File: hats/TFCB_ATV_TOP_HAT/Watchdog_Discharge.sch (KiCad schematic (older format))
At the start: 24 parts

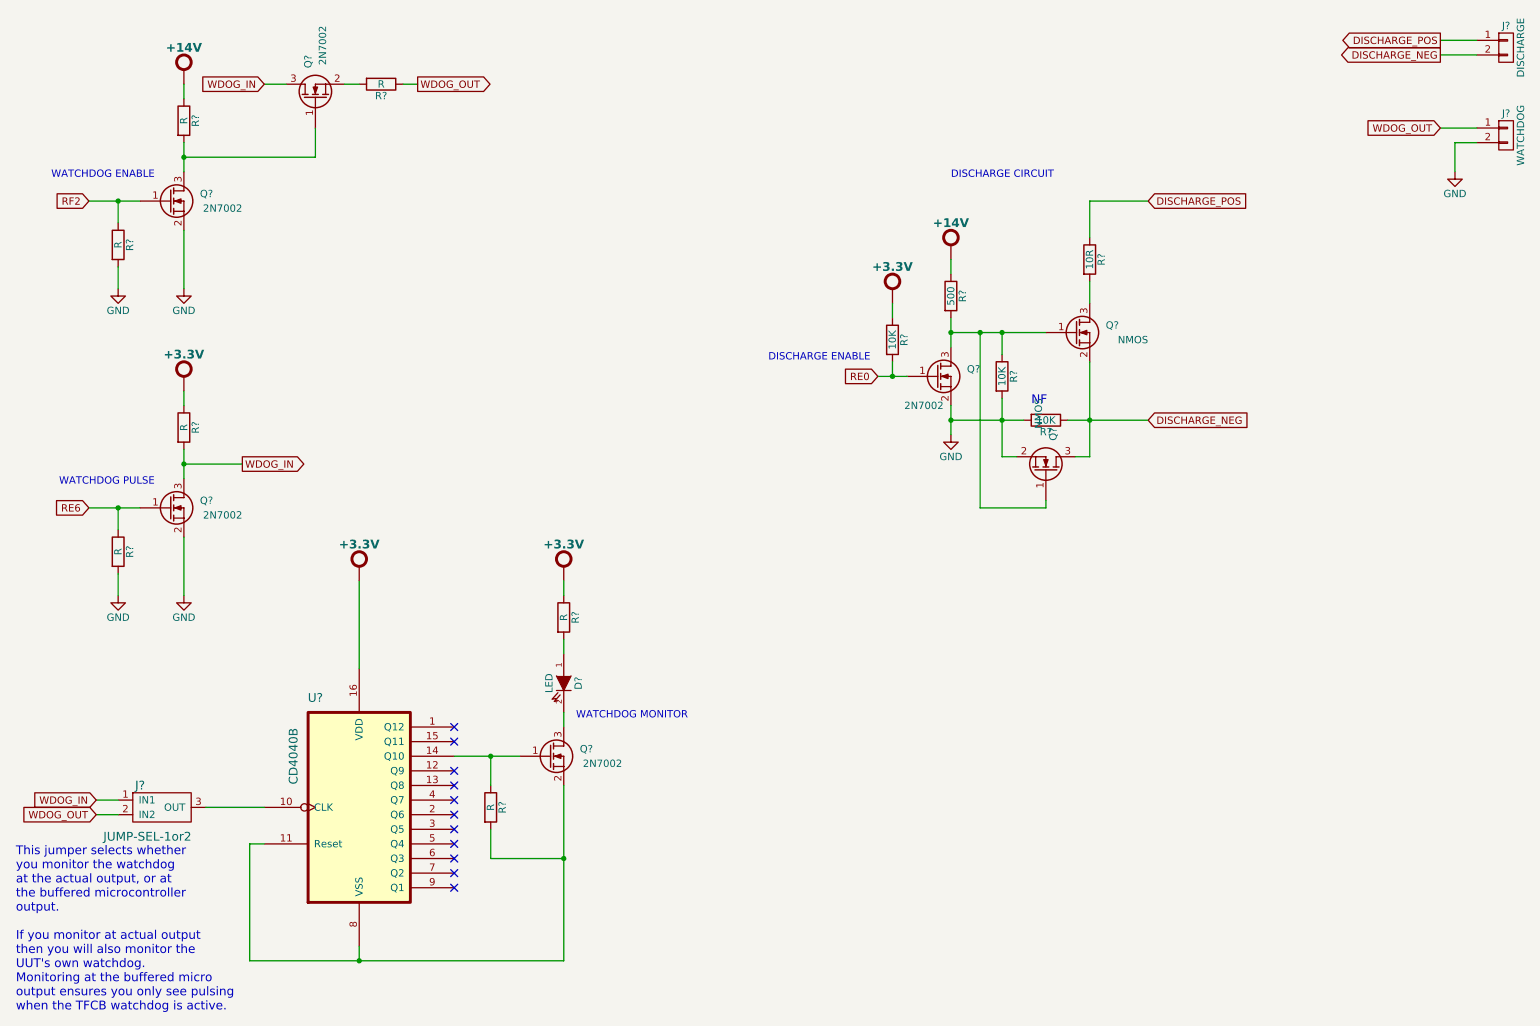
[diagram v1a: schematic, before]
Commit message: Added scanner trigger and current sense cct
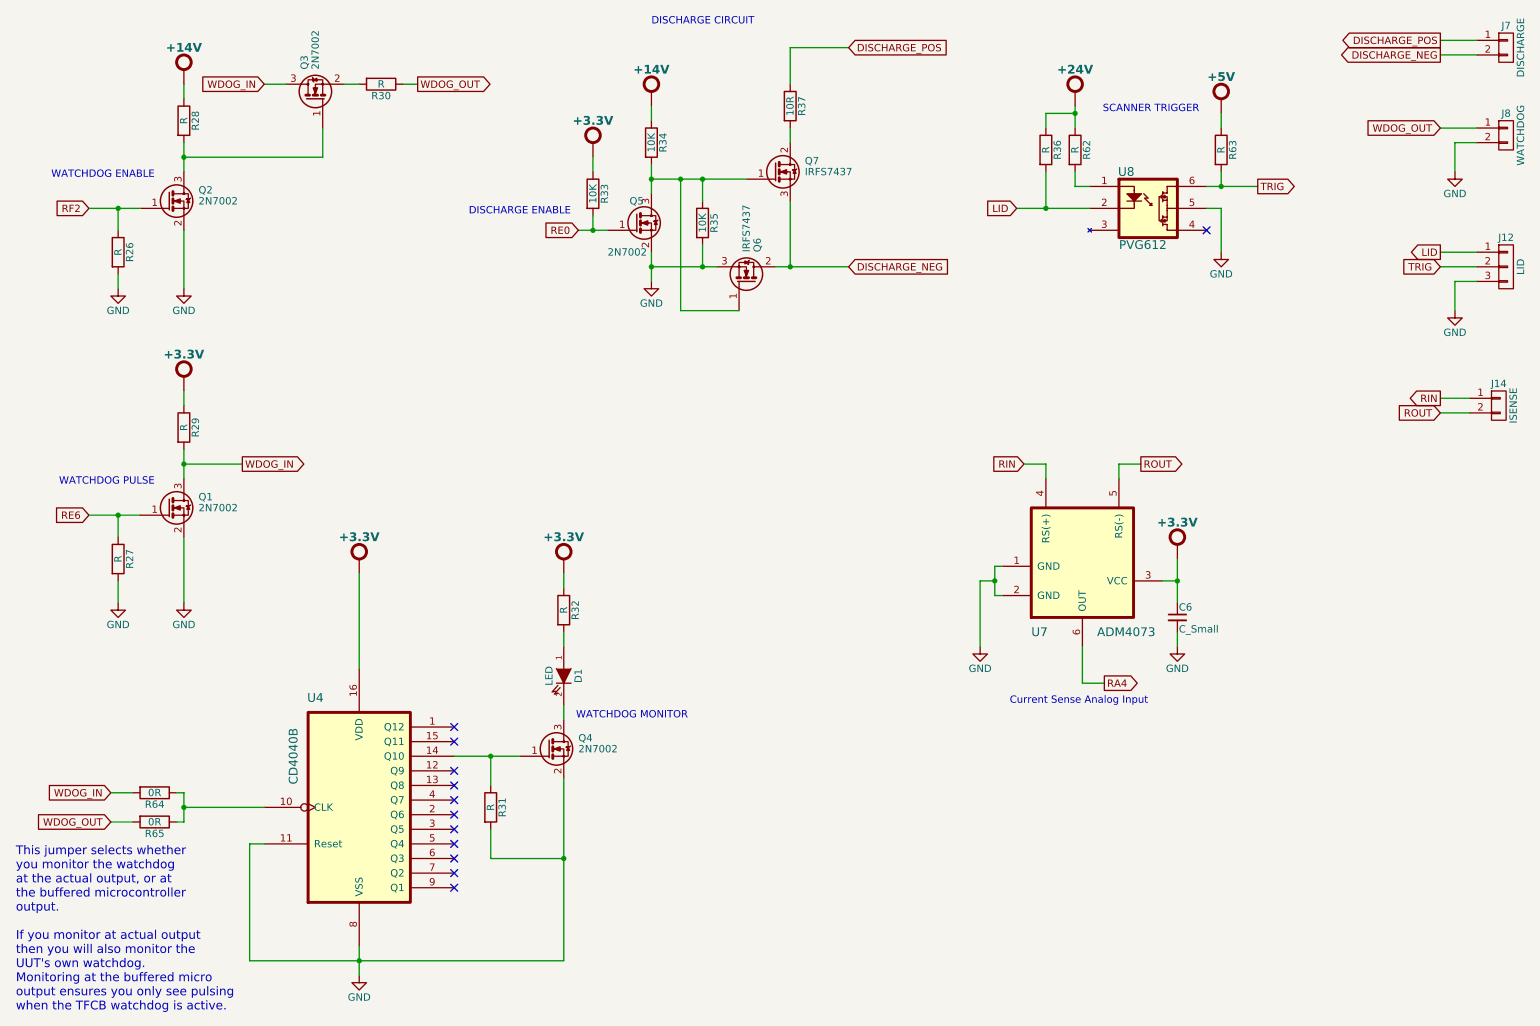
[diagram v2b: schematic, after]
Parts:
- removed J?: JUMP-SEL-1or2, symbol JUMP-SEL-1or2
- removed Q? (x5): 2N7002, symbol Q_NMOS_GSD-RESCUE-TFCB_ATV_HAT
- removed Q? (x2): NMOS, symbol Q_NMOS_GSD-RESCUE-TFCB_ATV_HAT
- removed R?: 10K, symbol R
- added C6: C_Small, Capacitors_SMD:C_0805_HandSoldering, symbol C_Small
- added J12: LID, bjh-kicad-connector-fp:Weidmuller-SL-5.08-Vertical-3Pole, symbol CONN_01X03
- added J14: ISENSE, bjh-kicad-connector-fp:Weidmuller-SL-5.08-Vertical-2Pole, symbol CONN_01X02
- added Q1, Q2, Q3, Q4, Q5: 2N7002, Housings_SOT-23_SOT-143_TSOT-6:SOT-23, symbol 2N7002
- added Q6, Q7: IRFS7437, SMD_Packages:DPAK-2, symbol IRFS7437
- added R36, R62, R63: R, Resistors_SMD:R_0805_HandSoldering, symbol R
- added R64, R65: 0R, Resistors_SMD:R_0805_HandSoldering, symbol R
- added U7: ADM4073, symbol ADM4073
- added U8: PVG612, symbol PVG612
- D1: renamed from D?; footprint (none) -> LEDs:LED-1206
- J7, J8: renamed from J?; footprint (none) -> bjh-kicad-connector-fp:Weidmuller-SL-5.08-Vertical-2Pole
- R26, R27, R28, R29, R30, R31, R32, R33, R35, R37: renamed from R?; footprint (none) -> Resistors_SMD:R_0805_HandSoldering
- R34: renamed from R?; value 500 -> 10K; footprint (none) -> Resistors_SMD:R_0805_HandSoldering
- gave numbers to parts that had none: 1
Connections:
- net +3.3V: now also C6.1, U7.3 (VCC)
- net DISCHARGE_NEG: now also Q6.2 (D), Q7.3 (S)
- net GND: now also R31.2, U4.11 (Reset), U4.8 (VSS), C6.2, J12.3 (P3), Q1.2 (S), Q2.2 (S), Q4.2 (S), Q5.2 (S), Q6.3 (S), U7.1 (GND), U7.2 (GND), U8.5
- net RE0: now also Q5.1 (G)
- net RE6: now also Q1.1 (G)
- net RF2: now also Q2.1 (G)
- net WDOG_IN: now also Q1.3 (D), Q3.3 (D), R64.2
- net WDOG_OUT: now also R65.2
- net at R28.2: now also Q2.3 (D), Q3.1 (G)
- net at R30.2: now also Q3.2 (S)
- net at U4.10 (CLK): now also R64.1, R65.1
- net at R31.1, U4.14 (Q10): now also Q4.1 (G)
- net at D1.2 (K): now also Q4.3 (D)
- net at R34.2, R35.1: now also Q5.3 (D), Q6.1 (G), Q7.1 (G)
- net at R37.2: now also Q7.2 (D)
- new net: R62.2, U8.1
- new net +24V: R36.1, R62.1
- new net +5V: R63.1
- new net LID: J12.1 (P1), R36.2, U8.2
- new net RA4: U7.6 (OUT)
- new net RIN: J14.1 (P1), U7.4 (RS(+))
- new net ROUT: J14.2 (P2), U7.5 (RS(-))
- new net TRIG: J12.2 (P2), R63.2, U8.6
- no-connect marks 11 -> 12
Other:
- note added: "Current Sense Analog Input"
- note added: "SCANNER TRIGGER"
- note removed: "NF"
- moved on the sheet: D1, R26, R27, R32, R33, R34, R35, R37

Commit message: latest updates
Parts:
- U4: footprint (none) -> Housings_SOIC:SOIC-14_3.9x8.7mm_Pitch1.27mm
- U7: footprint (none) -> Housings_SOT-23_SOT-143_TSOT-6:SC-70-6
- U8: footprint (none) -> bjh-kicad-switches-fp:IR-MicroSSRelay-6Pin-SMT
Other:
- moved on the sheet: C6, Q6, R35, U7
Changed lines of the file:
@@
 F 0 "U4" H 2700 6800 60  0000 C CNN
 F 1 "CD4040B" V 2550 6400 60  0000 C CNN
-F 2 "" H 3200 6050 60  0001 C CNN
+F 2 "Housings_SOIC:SOIC-14_3.9x8.7mm_Pitch1.27mm" H 3200 6050 60  0001 C CNN
 F 3 "" H 3200 6050 60  0000 C CNN
 	1    3000 6100
@@
 L R R35
 U 1 1 558B1ED2
-P 5350 2150
-F 0 "R35" V 5430 2150 50  0000 C CNN
-F 1 "10K" V 5350 2150 50  0000 C CNN
-F 2 "Resistors_SMD:R_0805_HandSoldering" V 5280 2150 30  0001 C CNN
-F 3 "" H 5350 2150 30  0000 C CNN
-	1    5350 2150
+P 5250 2150
+F 0 "R35" V 5330 2150 50  0000 C CNN
+F 1 "10K" V 5250 2150 50  0000 C CNN
+F 2 "Resistors_SMD:R_0805_HandSoldering" V 5180 2150 30  0001 C CNN
+F 3 "" H 5250 2150 30  0000 C CNN
+	1    5250 2150
 	1    0    0    -1
 $EndComp
@@
 L IRFS7437 Q6
 U 1 1 55B14706
-P 5650 2550
-F 0 "Q6" H 5850 2625 50  0000 L CNN
-F 1 "IRFS7437" H 5850 2550 50  0000 L CNN
-F 2 "SMD_Packages:DPAK-2" H 5850 2475 50  0001 L CIN
-F 3 "" H 5650 2550 50  0000 L CNN
-	1    5650 2550
-	0    1    -1   0
+P 5550 2350
+F 0 "Q6" H 5750 2425 50  0000 L CNN
+F 1 "IRFS7437" H 5750 2350 50  0000 L CNN
+F 2 "SMD_Packages:DPAK-2" H 5750 2275 50  0001 L CIN
+F 3 "" H 5550 2350 50  0000 L CNN
+	1    5550 2350
+	0    1    1    0
 $EndComp
 $Comp
@@
 L ADM4073 U7
 U 1 1 55B2418A
-P 7600 4100
-F 0 "U7" H 7600 3250 60  0000 L CNN
-F 1 "ADM4073" H 8050 3250 60  0000 L CNN
-F 2 "" H 7400 4000 60  0001 C CNN
-F 3 "" H 7400 4000 60  0000 C CNN
-	1    7600 4100
+P 8000 3150
+AR Path="/55B2418A" Ref="U7"  Part="1"
+AR Path="/558AFC77/55B2418A" Ref="U7"  Part="1"
+F 0 "U7" H 8000 2300 60  0000 L CNN
+F 1 "ADM4073" H 8450 2300 60  0000 L CNN
+F 2 "Housings_SOT-23_SOT-143_TSOT-6:SC-70-6" H 7800 3050 60  0001 C CNN
+F 3 "" H 7800 3050 60  0000 C CNN
+	1    8000 3150
 	1    0    0    -1
 $EndComp
@@
 L GND #PWR053
 U 1 1 55B243EE
-P 7250 5050
-F 0 "#PWR053" H 7250 4800 50  0001 C CNN
-F 1 "GND" H 7250 4900 50  0000 C CNN
-F 2 "" H 7250 5050 60  0000 C CNN
-F 3 "" H 7250 5050 60  0000 C CNN
-	1    7250 5050
+P 7650 4100
+F 0 "#PWR053" H 7650 3850 50  0001 C CNN
+F 1 "GND" H 7650 3950 50  0000 C CNN
+F 2 "" H 7650 4100 60  0000 C CNN
+F 3 "" H 7650 4100 60  0000 C CNN
+	1    7650 4100
 	1    0    0    -1
 $EndComp
@@
 L +3.3V_BJH #PWR054
 U 1 1 55B24749
-P 8600 4400
-F 0 "#PWR054" H 8600 4590 20  0001 C CNN
-F 1 "+3.3V_BJH" H 8600 4590 51  0001 C CNN
-F 2 "" H 8600 4400 60  0001 C CNN
-F 3 "" H 8600 4400 60  0001 C CNN
-F 4 "+3.3V" H 8600 4600 60  0000 C CNB "NAME"
-	1    8600 4400
+P 9000 3450
+F 0 "#PWR054" H 9000 3640 20  0001 C CNN
+F 1 "+3.3V_BJH" H 9000 3640 51  0001 C CNN
+F 2 "" H 9000 3450 60  0001 C CNN
+F 3 "" H 9000 3450 60  0001 C CNN
+F 4 "+3.3V" H 9000 3650 60  0000 C CNB "NAME"
+	1    9000 3450
 	1    0    0    -1
 $EndComp
@@
 L GND #PWR055
 U 1 1 55B247A4
-P 8600 5050
-F 0 "#PWR055" H 8600 4800 50  0001 C CNN
-F 1 "GND" H 8600 4900 50  0000 C CNN
-F 2 "" H 8600 5050 60  0000 C CNN
-F 3 "" H 8600 5050 60  0000 C CNN
-	1    8600 5050
+P 9000 4100
+F 0 "#PWR055" H 9000 3850 50  0001 C CNN
+F 1 "GND" H 9000 3950 50  0000 C CNN
+F 2 "" H 9000 4100 60  0000 C CNN
+F 3 "" H 9000 4100 60  0000 C CNN
+	1    9000 4100
 	1    0    0    -1
 $EndComp
@@
 L C_Small C6
 U 1 1 55B2492A
-P 8600 4850
-F 0 "C6" H 8610 4920 50  0000 L CNN
-F 1 "C_Small" H 8610 4770 50  0000 L CNN
-F 2 "Capacitors_SMD:C_0805_HandSoldering" H 8600 4850 60  0001 C CNN
-F 3 "" H 8600 4850 60  0000 C CNN
-	1    8600 4850
-	1    0    0    -1
-$EndComp
-Text GLabel 8100 5300 2    50   Output ~ 0
+P 9000 3900
+F 0 "C6" H 9010 3970 50  0000 L CNN
+F 1 "C_Small" H 9010 3820 50  0000 L CNN
+F 2 "Capacitors_SMD:C_0805_HandSoldering" H 9000 3900 60  0001 C CNN
+F 3 "" H 9000 3900 60  0000 C CNN
+	1    9000 3900
+	1    0    0    -1
+$EndComp
+Text GLabel 8500 4350 2    50   Output ~ 0
 RA4
-Text GLabel 7550 3800 0    50   Input ~ 0
+Text GLabel 7950 2850 0    50   Input ~ 0
 RIN
-Text GLabel 8350 3800 2    50   Output ~ 0
+Text GLabel 8750 2850 2    50   Output ~ 0
 ROUT
 $Comp
@@
 Text GLabel 10400 3450 0    50   Input ~ 0
 ROUT
-Text Notes 8400 5450 2    50   ~ 0
+Text Notes 8800 4500 2    50   ~ 0
 Current Sense Analog Input
 $Comp
@@
 F 0 "U8" H 8250 2000 60  0000 C CNN
 F 1 "PVG612" H 8200 1500 60  0000 L CNN
-F 2 "" H 8000 1900 60  0001 C CNN
+F 2 "bjh-kicad-switches-fp:IR-MicroSSRelay-6Pin-SMT" H 8000 1900 60  0001 C CNN
 F 3 "" H 8000 1900 60  0000 C CNN
 	1    8000 1900
@@
 	5950 1600 5950 1500
 Wire Wire Line
-	5000 2450 5450 2450
-Wire Wire Line
-	5350 2450 5350 2300
-Wire Wire Line
-	5850 2450 6350 2450
+	5750 2450 6350 2450
 Wire Wire Line
 	5950 2450 5950 2000
 Connection ~ 5950 2450
-Connection ~ 5350 2450
-Wire Wire Line
-	5600 2750 5200 2750
-Wire Wire Line
-	5200 2750 5200 1850
-Connection ~ 5200 1850
-Wire Wire Line
-	5350 2000 5350 1850
-Connection ~ 5350 1850
 Wire Wire Line
 	10400 2350 10650 2350
@@
 Connection ~ 8900 1900
 Wire Wire Line
-	7400 4500 7350 4500
-Wire Wire Line
-	7350 4500 7350 4700
-Wire Wire Line
-	7350 4700 7400 4700
-Wire Wire Line
-	7250 4600 7250 5050
-Wire Wire Line
-	7250 4600 7350 4600
-Connection ~ 7350 4600
-Wire Wire Line
-	8600 4950 8600 5050
-Wire Wire Line
-	8600 4450 8600 4750
-Wire Wire Line
-	8500 4600 8600 4600
-Connection ~ 8600 4600
-Wire Wire Line
-	8100 5300 7950 5300
-Wire Wire Line
-	7950 5300 7950 5050
-Wire Wire Line
-	7550 3800 7700 3800
-Wire Wire Line
-	7700 3800 7700 3900
-Wire Wire Line
-	8350 3800 8200 3800
-Wire Wire Line
-	8200 3800 8200 3900
+	7800 3550 7750 3550
+Wire Wire Line
+	7750 3550 7750 3750
+Wire Wire Line
+	7750 3750 7800 3750
+Wire Wire Line
+	7650 3650 7650 4100
+Wire Wire Line
+	7650 3650 7750 3650
+Connection ~ 7750 3650
+Wire Wire Line
+	9000 4000 9000 4100
+Wire Wire Line
+	9000 3500 9000 3800
+Wire Wire Line
+	8900 3650 9000 3650
+Connection ~ 9000 3650
+Wire Wire Line
+	8500 4350 8350 4350
+Wire Wire Line
+	8350 4350 8350 4100
+Wire Wire Line
+	7950 2850 8100 2850
+Wire Wire Line
+	8100 2850 8100 2950
+Wire Wire Line
+	8750 2850 8600 2850
+Wire Wire Line
+	8600 2850 8600 2950
 Wire Wire Line
 	10400 3350 10600 3350
@@
 	1800 6250 1750 6250
 Connection ~ 1800 6150
+Wire Wire Line
+	5000 2450 5350 2450
+Wire Wire Line
+	5500 2150 5500 1850
+Connection ~ 5500 1850
+Wire Wire Line
+	5250 2000 5250 1850
+Connection ~ 5250 1850
+Wire Wire Line
+	5250 2300 5250 2450
+Connection ~ 5250 2450
 $EndSCHEMATC

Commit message: More work on TFCB
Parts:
- R37: footprint Resistors_SMD:R_0805_HandSoldering -> bjh-kicad-rcld-fp:PWR5322_SMD
- U4: footprint Housings_SOIC:SOIC-14_3.9x8.7mm_Pitch1.27mm -> Housings_SOIC:SOIC-16_3.9x9.9mm_Pitch1.27mm
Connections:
- net RE0 renamed RJ3
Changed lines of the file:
@@
 $EndComp
 $Comp
-L +14V_BJH #PWR036
+L +14V_BJH #PWR037
 U 1 1 558AFF37
 P 1800 1150
-F 0 "#PWR036" H 1800 1340 20  0001 C CNN
+F 0 "#PWR037" H 1800 1340 20  0001 C CNN
 F 1 "+14V_BJH" H 1800 1340 51  0001 C CNN
 F 2 "" H 1800 1150 60  0001 C CNN
@@
 WATCHDOG ENABLE
 $Comp
-L GND #PWR037
+L GND #PWR038
 U 1 1 558B03D6
 P 1800 2600
-F 0 "#PWR037" H 1800 2350 50  0001 C CNN
+F 0 "#PWR038" H 1800 2350 50  0001 C CNN
 F 1 "GND" H 1800 2450 50  0000 C CNN
 F 2 "" H 1800 2600 60  0000 C CNN
@@
 $EndComp
 $Comp
-L GND #PWR038
+L GND #PWR039
 U 1 1 558B0404
 P 1350 2600
-F 0 "#PWR038" H 1350 2350 50  0001 C CNN
+F 0 "#PWR039" H 1350 2350 50  0001 C CNN
 F 1 "GND" H 1350 2450 50  0000 C CNN
 F 2 "" H 1350 2600 60  0000 C CNN
@@
 WATCHDOG PULSE
 $Comp
-L GND #PWR039
+L GND #PWR040
 U 1 1 558B0737
 P 1800 4750
-F 0 "#PWR039" H 1800 4500 50  0001 C CNN
+F 0 "#PWR040" H 1800 4500 50  0001 C CNN
 F 1 "GND" H 1800 4600 50  0000 C CNN
 F 2 "" H 1800 4750 60  0000 C CNN
@@
 $EndComp
 $Comp
-L GND #PWR040
+L GND #PWR041
 U 1 1 558B073E
 P 1350 4750
-F 0 "#PWR040" H 1350 4500 50  0001 C CNN
+F 0 "#PWR041" H 1350 4500 50  0001 C CNN
 F 1 "GND" H 1350 4600 50  0000 C CNN
 F 2 "" H 1350 4750 60  0000 C CNN
@@
 $EndComp
 $Comp
-L +3.3V_BJH #PWR041
+L +3.3V_BJH #PWR042
 U 1 1 558B07AC
 P 1800 3250
-F 0 "#PWR041" H 1800 3440 20  0001 C CNN
+F 0 "#PWR042" H 1800 3440 20  0001 C CNN
 F 1 "+3.3V_BJH" H 1800 3440 51  0001 C CNN
 F 2 "" H 1800 3250 60  0001 C CNN
@@
 Text GLabel 2200 3800 2    50   Output ~ 0
 WDOG_IN
-$Comp
-L CD4040B U4
-U 1 1 558B0913
-P 3000 6100
-F 0 "U4" H 2700 6800 60  0000 C CNN
-F 1 "CD4040B" V 2550 6400 60  0000 C CNN
-F 2 "Housings_SOIC:SOIC-14_3.9x8.7mm_Pitch1.27mm" H 3200 6050 60  0001 C CNN
-F 3 "" H 3200 6050 60  0000 C CNN
-	1    3000 6100
-	1    0    0    -1
-$EndComp
 Text GLabel 1300 6050 0    50   Input ~ 0
 WDOG_IN
@@
 $EndComp
 $Comp
-L +3.3V_BJH #PWR042
+L +3.3V_BJH #PWR043
 U 1 1 558B0DD9
 P 4400 4500
-F 0 "#PWR042" H 4400 4690 20  0001 C CNN
+F 0 "#PWR043" H 4400 4690 20  0001 C CNN
 F 1 "+3.3V_BJH" H 4400 4690 51  0001 C CNN
 F 2 "" H 4400 4500 60  0001 C CNN
@@
 $EndComp
 $Comp
-L +3.3V_BJH #PWR043
+L +3.3V_BJH #PWR044
 U 1 1 558B0FE6
 P 3000 4500
-F 0 "#PWR043" H 3000 4690 20  0001 C CNN
+F 0 "#PWR044" H 3000 4690 20  0001 C CNN
 F 1 "+3.3V_BJH" H 3000 4690 51  0001 C CNN
 F 2 "" H 3000 4500 60  0001 C CNN
@@
 WDOG_OUT
 Text GLabel 4500 2200 0    50   Input ~ 0
-RE0
+RJ3
 $Comp
 L R R33
@@
 $EndComp
 $Comp
-L +3.3V_BJH #PWR044
+L +3.3V_BJH #PWR045
 U 1 1 558B1B6B
 P 4600 1650
-F 0 "#PWR044" H 4600 1840 20  0001 C CNN
+F 0 "#PWR045" H 4600 1840 20  0001 C CNN
 F 1 "+3.3V_BJH" H 4600 1840 51  0001 C CNN
 F 2 "" H 4600 1650 60  0001 C CNN
@@
 $EndComp
 $Comp
-L +14V_BJH #PWR045
+L +14V_BJH #PWR046
 U 1 1 558B1CA1
 P 5000 1300
-F 0 "#PWR045" H 5000 1490 20  0001 C CNN
+F 0 "#PWR046" H 5000 1490 20  0001 C CNN
 F 1 "+14V_BJH" H 5000 1490 51  0001 C CNN
 F 2 "" H 5000 1300 60  0001 C CNN
@@
 $EndComp
 $Comp
-L GND #PWR046
+L GND #PWR047
 U 1 1 558B20E6
 P 5000 2550
-F 0 "#PWR046" H 5000 2300 50  0001 C CNN
+F 0 "#PWR047" H 5000 2300 50  0001 C CNN
 F 1 "GND" H 5000 2400 50  0000 C CNN
 F 2 "" H 5000 2550 60  0000 C CNN
@@
 F 0 "R37" V 6030 1350 50  0000 C CNN
 F 1 "10R" V 5950 1350 50  0000 C CNN
-F 2 "Resistors_SMD:R_0805_HandSoldering" V 5880 1350 30  0001 C CNN
+F 2 "bjh-kicad-rcld-fp:PWR5322_SMD" V 5880 1350 30  0001 C CNN
 F 3 "" H 5950 1350 30  0000 C CNN
 	1    5950 1350
@@
 $EndComp
 $Comp
-L GND #PWR047
+L GND #PWR048
 U 1 1 558B6642
 P 10500 1800
-F 0 "#PWR047" H 10500 1550 50  0001 C CNN
+F 0 "#PWR048" H 10500 1550 50  0001 C CNN
 F 1 "GND" H 10500 1650 50  0000 C CNN
 F 2 "" H 10500 1800 60  0000 C CNN
@@
 NoConn ~ 3650 6700
 $Comp
-L GND #PWR048
+L GND #PWR049
 U 1 1 55AFC11C
 P 3000 7300
-F 0 "#PWR048" H 3000 7050 50  0001 C CNN
+F 0 "#PWR049" H 3000 7050 50  0001 C CNN
 F 1 "GND" H 3000 7150 50  0000 C CNN
 F 2 "" H 3000 7300 60  0000 C CNN
@@
 $EndComp
 $Comp
-L GND #PWR049
+L GND #PWR050
 U 1 1 55B21D95
 P 10500 2750
-F 0 "#PWR049" H 10500 2500 50  0001 C CNN
+F 0 "#PWR050" H 10500 2500 50  0001 C CNN
 F 1 "GND" H 10500 2600 50  0000 C CNN
 F 2 "" H 10500 2750 60  0000 C CNN
@@
 $EndComp
 $Comp
-L +24V_BJH #PWR050
+L +24V_BJH #PWR051
 U 1 1 55B22BD7
 P 7900 1300
-F 0 "#PWR050" H 7900 1490 20  0001 C CNN
+F 0 "#PWR051" H 7900 1490 20  0001 C CNN
 F 1 "+24V_BJH" H 7900 1490 51  0001 C CNN
 F 2 "" H 7900 1300 60  0001 C CNN
@@
 $EndComp
 $Comp
-L +5V_BJH #PWR051
+L +5V_BJH #PWR052
 U 1 1 55B2341E
 P 8900 1350
-F 0 "#PWR051" H 8900 1540 20  0001 C CNN
+F 0 "#PWR052" H 8900 1540 20  0001 C CNN
 F 1 "+5V_BJH" H 8900 1540 51  0001 C CNN
 F 2 "" H 8900 1350 60  0001 C CNN
@@
 $EndComp
 $Comp
-L GND #PWR052
+L GND #PWR053
 U 1 1 55B23559
 P 8900 2350
-F 0 "#PWR052" H 8900 2100 50  0001 C CNN
+F 0 "#PWR053" H 8900 2100 50  0001 C CNN
 F 1 "GND" H 8900 2200 50  0000 C CNN
 F 2 "" H 8900 2350 60  0000 C CNN
@@
 $EndComp
 $Comp
-L GND #PWR053
+L GND #PWR054
 U 1 1 55B243EE
 P 7650 4100
-F 0 "#PWR053" H 7650 3850 50  0001 C CNN
+F 0 "#PWR054" H 7650 3850 50  0001 C CNN
 F 1 "GND" H 7650 3950 50  0000 C CNN
 F 2 "" H 7650 4100 60  0000 C CNN
@@
 $EndComp
 $Comp
-L +3.3V_BJH #PWR054
+L +3.3V_BJH #PWR055
 U 1 1 55B24749
 P 9000 3450
-F 0 "#PWR054" H 9000 3640 20  0001 C CNN
+F 0 "#PWR055" H 9000 3640 20  0001 C CNN
 F 1 "+3.3V_BJH" H 9000 3640 51  0001 C CNN
 F 2 "" H 9000 3450 60  0001 C CNN
@@
 $EndComp
 $Comp
-L GND #PWR055
+L GND #PWR056
 U 1 1 55B247A4
 P 9000 4100
-F 0 "#PWR055" H 9000 3850 50  0001 C CNN
+F 0 "#PWR056" H 9000 3850 50  0001 C CNN
 F 1 "GND" H 9000 3950 50  0000 C CNN
 F 2 "" H 9000 4100 60  0000 C CNN
@@
 	5250 2300 5250 2450
 Connection ~ 5250 2450
+$Comp
+L CD4040B U4
+U 1 1 55B8BA7C
+P 3000 6100
+F 0 "U4" H 2700 6800 60  0000 C CNN
+F 1 "CD4040B" V 2550 6400 60  0000 C CNN
+F 2 "Housings_SOIC:SOIC-16_3.9x9.9mm_Pitch1.27mm" H 3200 6050 60  0001 C CNN
+F 3 "" H 3200 6050 60  0000 C CNN
+	1    3000 6100
+	1    0    0    -1
+$EndComp
 $EndSCHEMATC
